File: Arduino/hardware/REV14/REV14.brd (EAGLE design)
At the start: 100 x 50 mm, 37 parts, among them IC1 LTC3525, IC2 ATMEGA168-AU, Q1 32768Hz, U1 RN2483, U2 TMP112, X1 SMA-142-0701-881/886, X2 SMA-142-0701-881/886

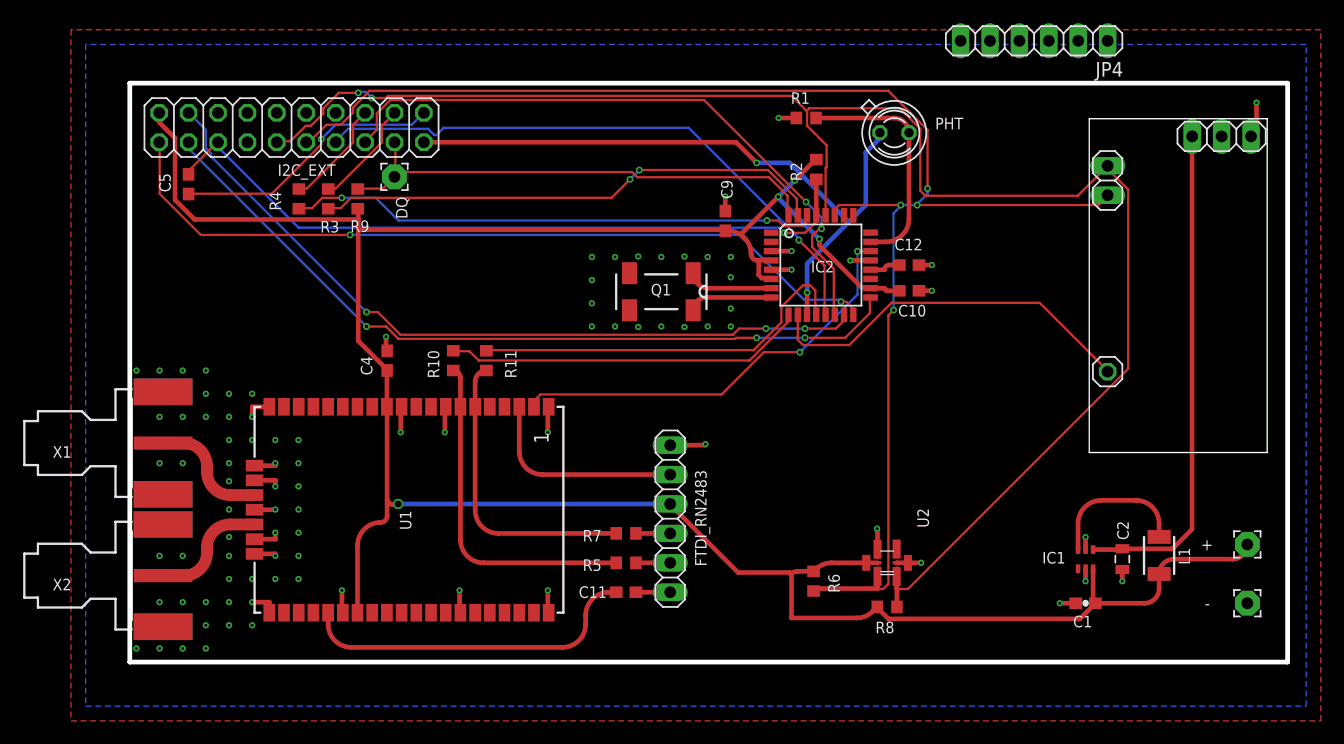
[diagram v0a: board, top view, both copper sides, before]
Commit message: reservered space for mobdet on rev 14
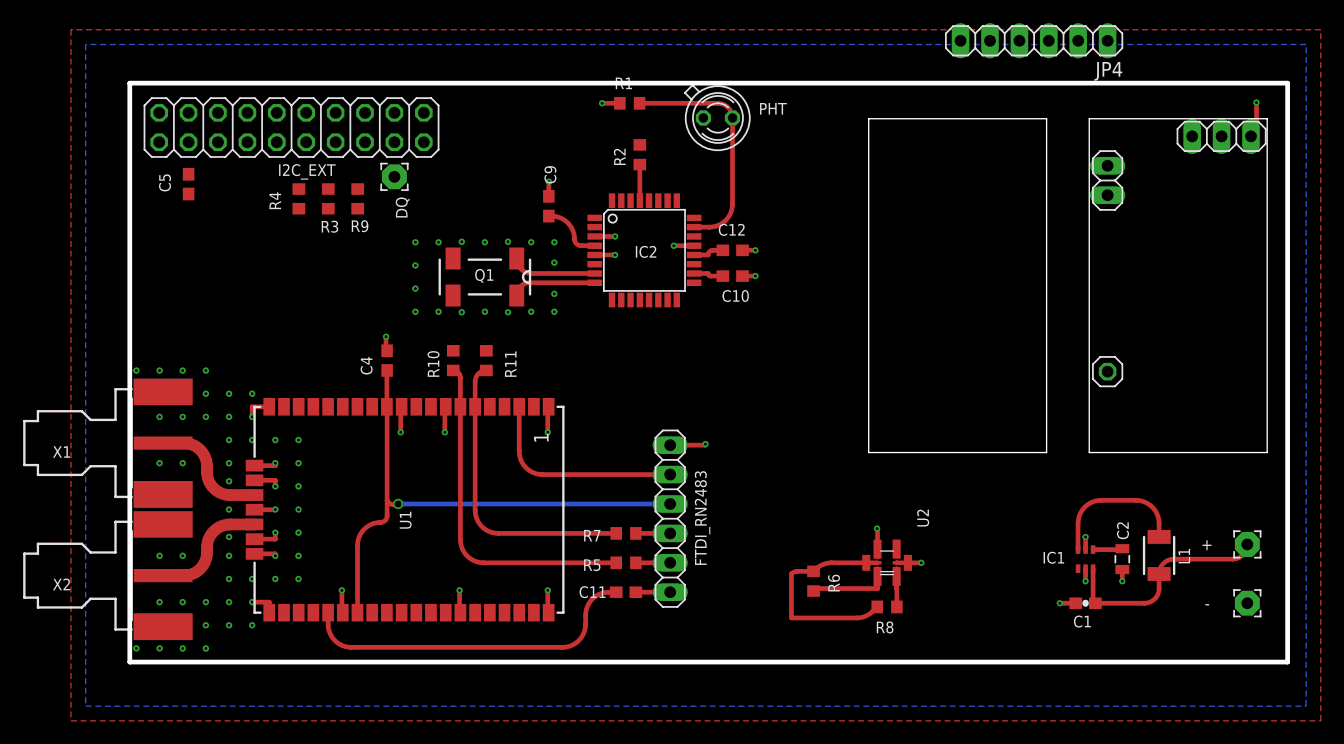
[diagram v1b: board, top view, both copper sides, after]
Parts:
- moved PHT 15.3 mm to (50.8, 47.0)
- moved C10 15.3 mm to (52.1, 33.3)
- moved C12 15.3 mm to (52.1, 35.6)
- moved C9 15.3 mm to (36.2, 39.4)
- moved R1 15.3 mm to (43.2, 48.3)
- moved R2 15.3 mm to (44.0, 43.8)
- moved IC2 15.3 mm to (44.5, 35.6)
- moved Q1 15.3 mm to (30.7, 33.3)
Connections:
- new net PHONE: IC2.24
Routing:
- net SCL: track 141.4 -> 3.32 mm, vias 2 -> 0
- net VCC: track 220.1 -> 92.3 mm, vias 4 -> 1
- net SDA: track 130.3 -> 7.34 mm, vias 4 -> 0
- net SPI_MISO: track 69.0 -> 0.00 mm, vias 2 -> 0
- net SPI_SCK: track 68.6 -> 0.00 mm, vias 3 -> 0
- net SPI_MOSI: track 66.7 -> 0.00 mm, vias 3 -> 0
- net RESET: track 63.1 -> 3.11 mm, vias 1 -> 0
- net IO_POWER_UP: track 57.9 -> 0.00 mm, vias 2 -> 0
- net SPI_NSS: track 55.6 -> 0.00 mm, vias 2 -> 0
- net RFM_IRQ: track 52.6 -> 0.00 mm, vias 1 -> 0
- net TX: track 46.0 -> 0.00 mm, vias 2 -> 0
- net RX: track 44.4 -> 0.00 mm, vias 2 -> 0
- net D2: track 43.7 -> 0.00 mm
- net VCC1: track 43.2 -> 2.56 mm
- net RN2483_UART_RTS: track 37.1 -> 0.00 mm, vias 2 -> 0
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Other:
- outline, holes or cut-outs redrawn

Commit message: added rough mobdect to rev14
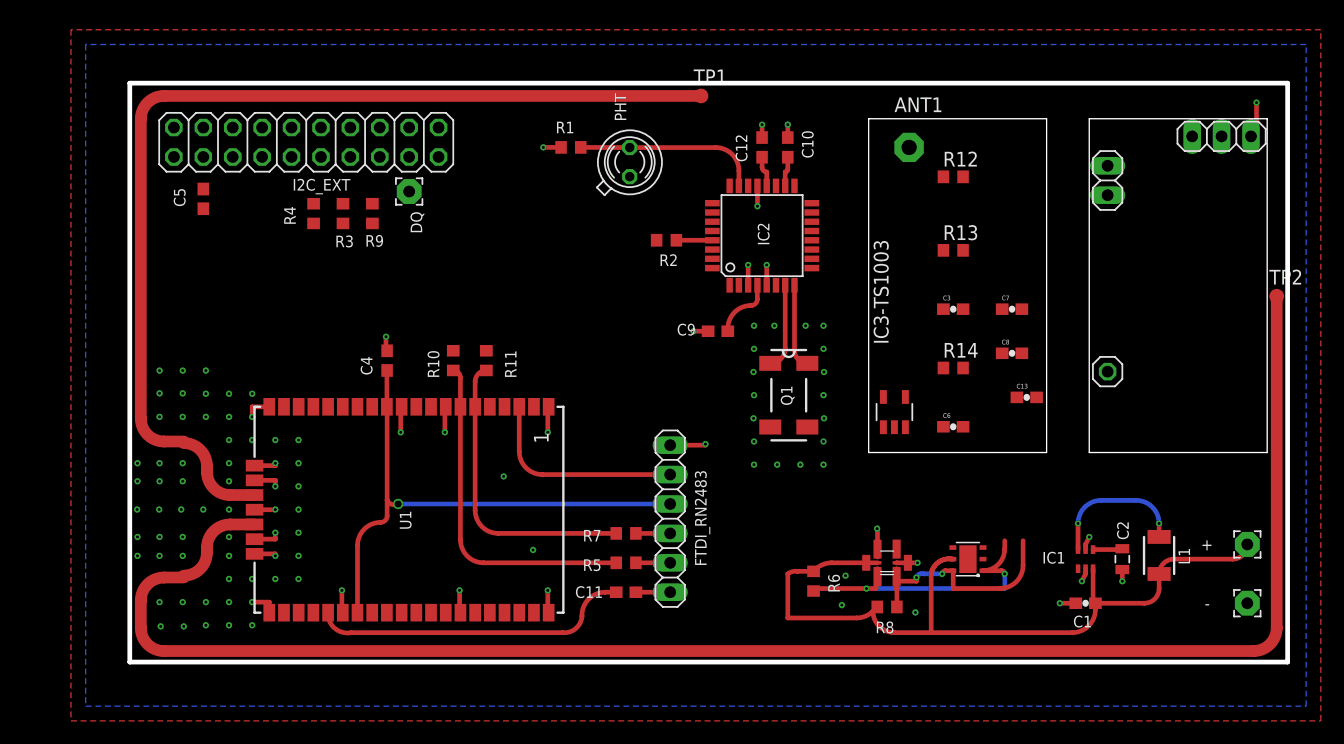
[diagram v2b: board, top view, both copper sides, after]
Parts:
- removed JP4: (no value), pinhead:1X06
- removed X1, X2: SMA-142-0701-881/886, con-coax:J502-ND-142-0701-881/886
- added ANT1: (no value), discrete:PAD-01
- added C13, C3, C6, C7, C8: 1µ, SparkFun:0603-CAP
- added IC3-TS1003: LM321MF, linear:SOT23-5
- added R12, R13, R14: 4.7K, resistor:R0603
- added TP1, TP2: TPB1,27, testpad:B1,27
- added U$4: SHT21, SHT21:SHT21
- moved Q1 28.2 mm to (56.9, 23.1), turned to 270 degrees
- moved C9 18.2 mm to (50.8, 28.6), turned to 180 degrees
- moved C10 12.1 mm to (56.8, 44.5), turned to 90 degrees
- moved IC2 10.2 mm to (54.6, 36.8), turned to 90 degrees
- moved C12 9.25 mm to (54.6, 44.5), turned to 90 degrees
- moved PHT 8.52 mm to (43.2, 43.2), turned to 45 degrees
- moved R2 7.74 mm to (46.4, 36.4), turned to 0 degrees
- moved R1 6.35 mm to (38.1, 44.5)
- moved R3 1.80 mm to (18.4, 38.7)
- moved R4 1.80 mm to (15.9, 38.7)
- moved R9 1.80 mm to (21.0, 38.7)
- moved C5 1.80 mm to (6.35, 40.0)
- moved DQ 1.80 mm to (24.1, 40.6)
- moved I2C_EXT 1.80 mm to (15.2, 44.9)
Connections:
- new net N$11: C13.1, C6.1, C8.2, IC3-TS1003.3, R12.2
- new net N$12: C3.2, IC3-TS1003.4, R12.1
- new net N$13: C3.1, C7.1, C8.1, R13.2
- new net N$14: C6.2, C7.2, IC3-TS1003.1, R13.1, R14.2
- new net N$15: ANT1.1, C13.2
- new net V+: IC3-TS1003.5
- new net V-: IC3-TS1003.2
- net GND: now also U$4.2, U$4.P$1; no longer X1.G@1, X1.G@2, X1.G@3, X1.G@4, X2.G@1, X2.G@2, X2.G@3, X2.G@4
- net N$22: now also TP1.TP; no longer X1.1
- net N$33: now also TP2.TP; no longer X2.1
- net SCL: now also U$4.6
- net SDA: now also U$4.1
- net VCC: now also R14.1, U$4.5
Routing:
- net N$33: track 9.97 -> 143.6 mm
- net N$22: track 10.0 -> 88.0 mm
- net VCC: track 92.3 -> 123.8 mm
- net SDA: track 7.34 -> 25.8 mm, vias 0 -> 2
- net SCL: track 3.32 -> 19.2 mm, vias 0 -> 2
- net LDR: track 20.1 -> 15.8 mm
- net RN2483_RESET: track 29.1 -> 27.1 mm
- net GND: track 55.3 -> 55.1 mm, vias 91 -> 96
- net N$10: vias 0 -> 2

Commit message: rev14 prerouting
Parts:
- removed ANT1: (no value), discrete:PAD-01
- removed C13, C3, C6, C7, C8: 1µ, SparkFun:0603-CAP
- removed IC3-TS1003: LM321MF, linear:SOT23-5
- removed R12, R13, R14: 4.7K, resistor:R0603
- added JP4: (no value), pinhead:1X03
- C2: device SparkFun:0805 -> rcl:C0603
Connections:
- removed net N$11: C13.1, C6.1, C8.2, IC3-TS1003.3, R12.2
- removed net N$12: C3.2, IC3-TS1003.4, R12.1
- removed net N$13: C3.1, C7.1, C8.1, R13.2
- removed net N$14: C6.2, C7.2, IC3-TS1003.1, R13.1, R14.2
- removed net N$15: ANT1.1, C13.2
- removed net V+: IC3-TS1003.5
- removed net V-: IC3-TS1003.2
- net CHG_PUMP: now also IC2.26
- net GND: now also JP4.3
- net RN2483_RESET: now also IC2.25
- net RN2483_UART_CTS: now also IC2.19
- net VCC: no longer R14.1
- net VCC1: now also JP4.1

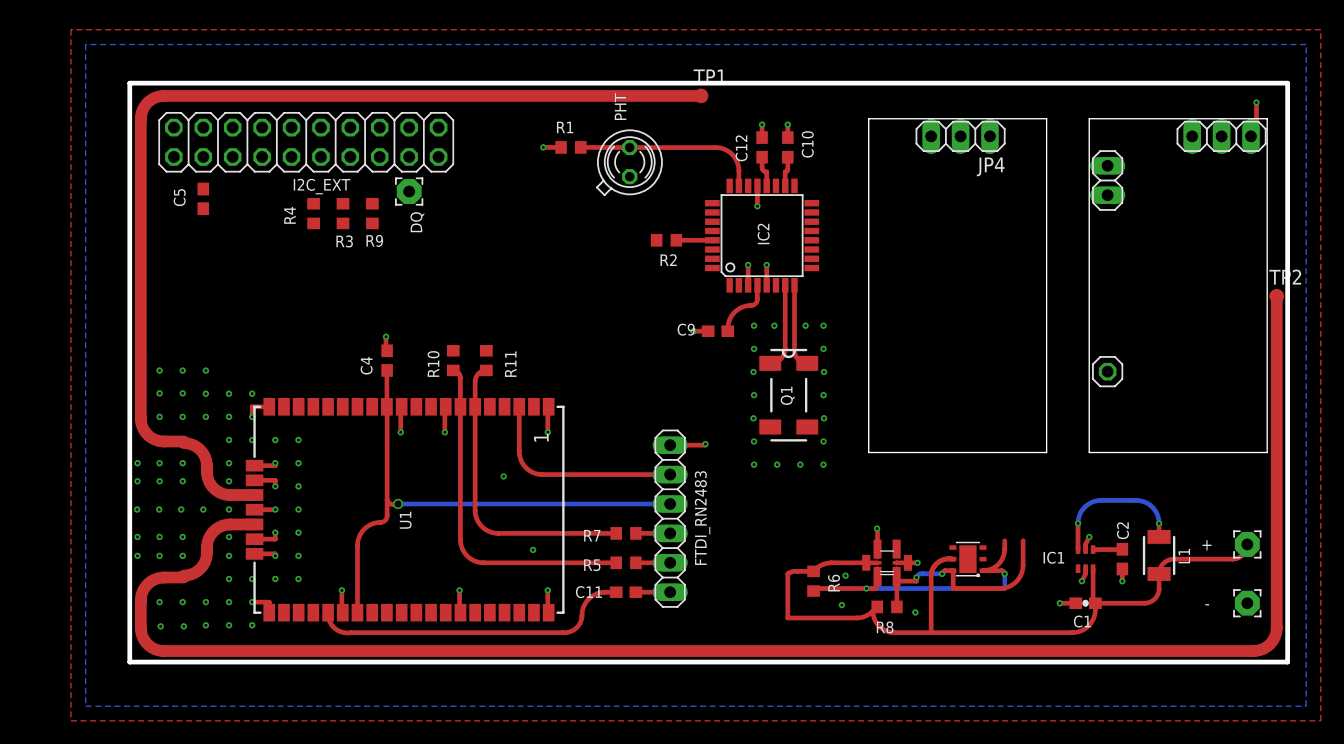
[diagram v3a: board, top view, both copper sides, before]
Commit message: more ground plane on rev14
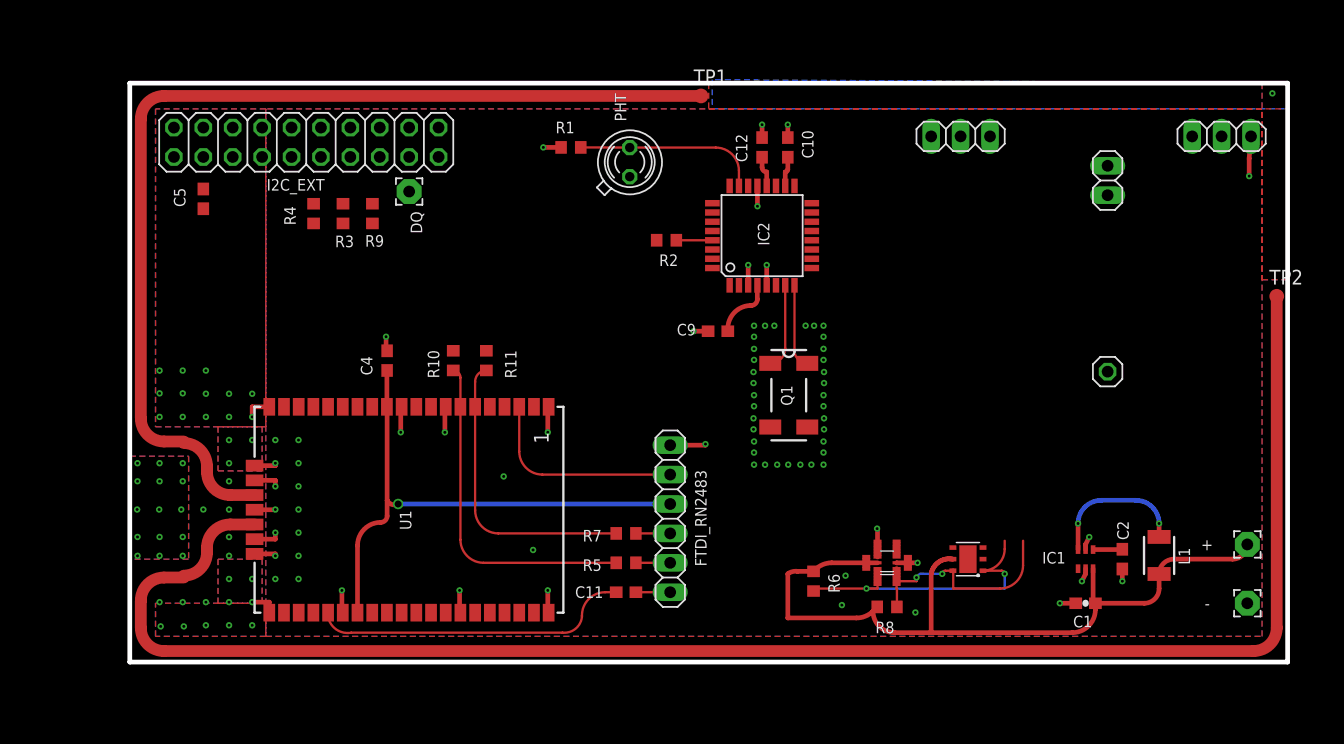
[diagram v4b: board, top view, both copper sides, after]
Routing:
- net GND: vias 96 -> 125
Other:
- outline, holes or cut-outs redrawn

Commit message: rev 14 update
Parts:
- added R12, R13, R14, R15, R16, R17, R18: 4.7K, resistor:R0603
- JP4: device pinhead:1X03 -> pinhead:1X04
- moved C5 92.4 mm to (94.0, 10.8), turned to 90 degrees
- moved I2C_EXT 80.0 mm to (85.1, 5.91), turned to 180 degrees
- moved R4 73.6 mm to (84.5, 12.1), turned to 270 degrees
- moved R3 68.9 mm to (81.9, 12.1), turned to 270 degrees
- moved R9 64.2 mm to (79.4, 12.1), turned to 90 degrees
- moved DQ 60.3 mm to (76.2, 10.2), turned to 90 degrees
- moved TP1 43.7 mm to (93.0, 48.9)
- moved - 41.9 mm to (54.6, 6.35), turned to 270 degrees
- moved R1 38.2 mm to (35.6, 6.35), turned to 270 degrees
- moved C11 37.2 mm to (5.71, 7.30), turned to 270 degrees
- moved + 37.0 mm to (59.7, 6.35), turned to 270 degrees
- moved R6 36.9 mm to (56.5, 43.8), turned to 180 degrees
- moved FTDI_RN2483 35.7 mm to (12.1, 3.49), turned to 180 degrees
- moved R5 34.6 mm to (8.26, 7.30), turned to 270 degrees
- moved R8 34.5 mm to (54.3, 37.5), turned to 90 degrees
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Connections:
- new net N$11: IC2.19, R12.2
- new net N$12: IC2.22, R13.2
- new net N$13: IC2.25, R14.2
- new net N$14: FTDI_RN2483.2, R17.1
- new net N$16: JP4.2, R16.1
- new net N$17: I2C_EXT.12, R18.2
- net GND: now also R17.2, R18.1; no longer I2C_EXT.12
- net PHONE: now also R16.2
- net RN2483_RESET: now also R14.1, R15.2; no longer IC2.25
- net RN2483_UART_CTS: now also R12.1; no longer FTDI_RN2483.2, IC2.19
- net RN2483_UART_RTS: now also R13.1; no longer IC2.22
- net VCC: now also JP4.4, R15.1; no longer FTDI_RN2483.3
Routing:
- net VCC: track 123.8 -> 100.3 mm
- net N$33: track 143.6 -> 156.1 mm
- net RN2483_UART_CTS: track 17.7 -> 6.68 mm
- net LDR: track 15.8 -> 19.3 mm
- net N$22: track 88.0 -> 85.5 mm
- net RN2483_UART_TX: track 25.5 -> 24.2 mm
- net RN2483_UART_RX: track 29.2 -> 27.9 mm
- net RN2483_RESET: track 27.1 -> 26.4 mm
- net GND: track 55.2 -> 55.4 mm, vias 125 -> 113
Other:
- board text added: "*"
- board text added: "* Do NOT Pop."
